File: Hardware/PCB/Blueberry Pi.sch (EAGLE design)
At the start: 172 parts, among them IC3 AT45DB161D, J1 TRANSFLASH-LOCK, J2 AUDIO_JACK_SMD, J3 40PINFPCH15-1LW, Q1 24Mhz, Q2 32kHz, X1 USB-B-S, X3 52745-2290

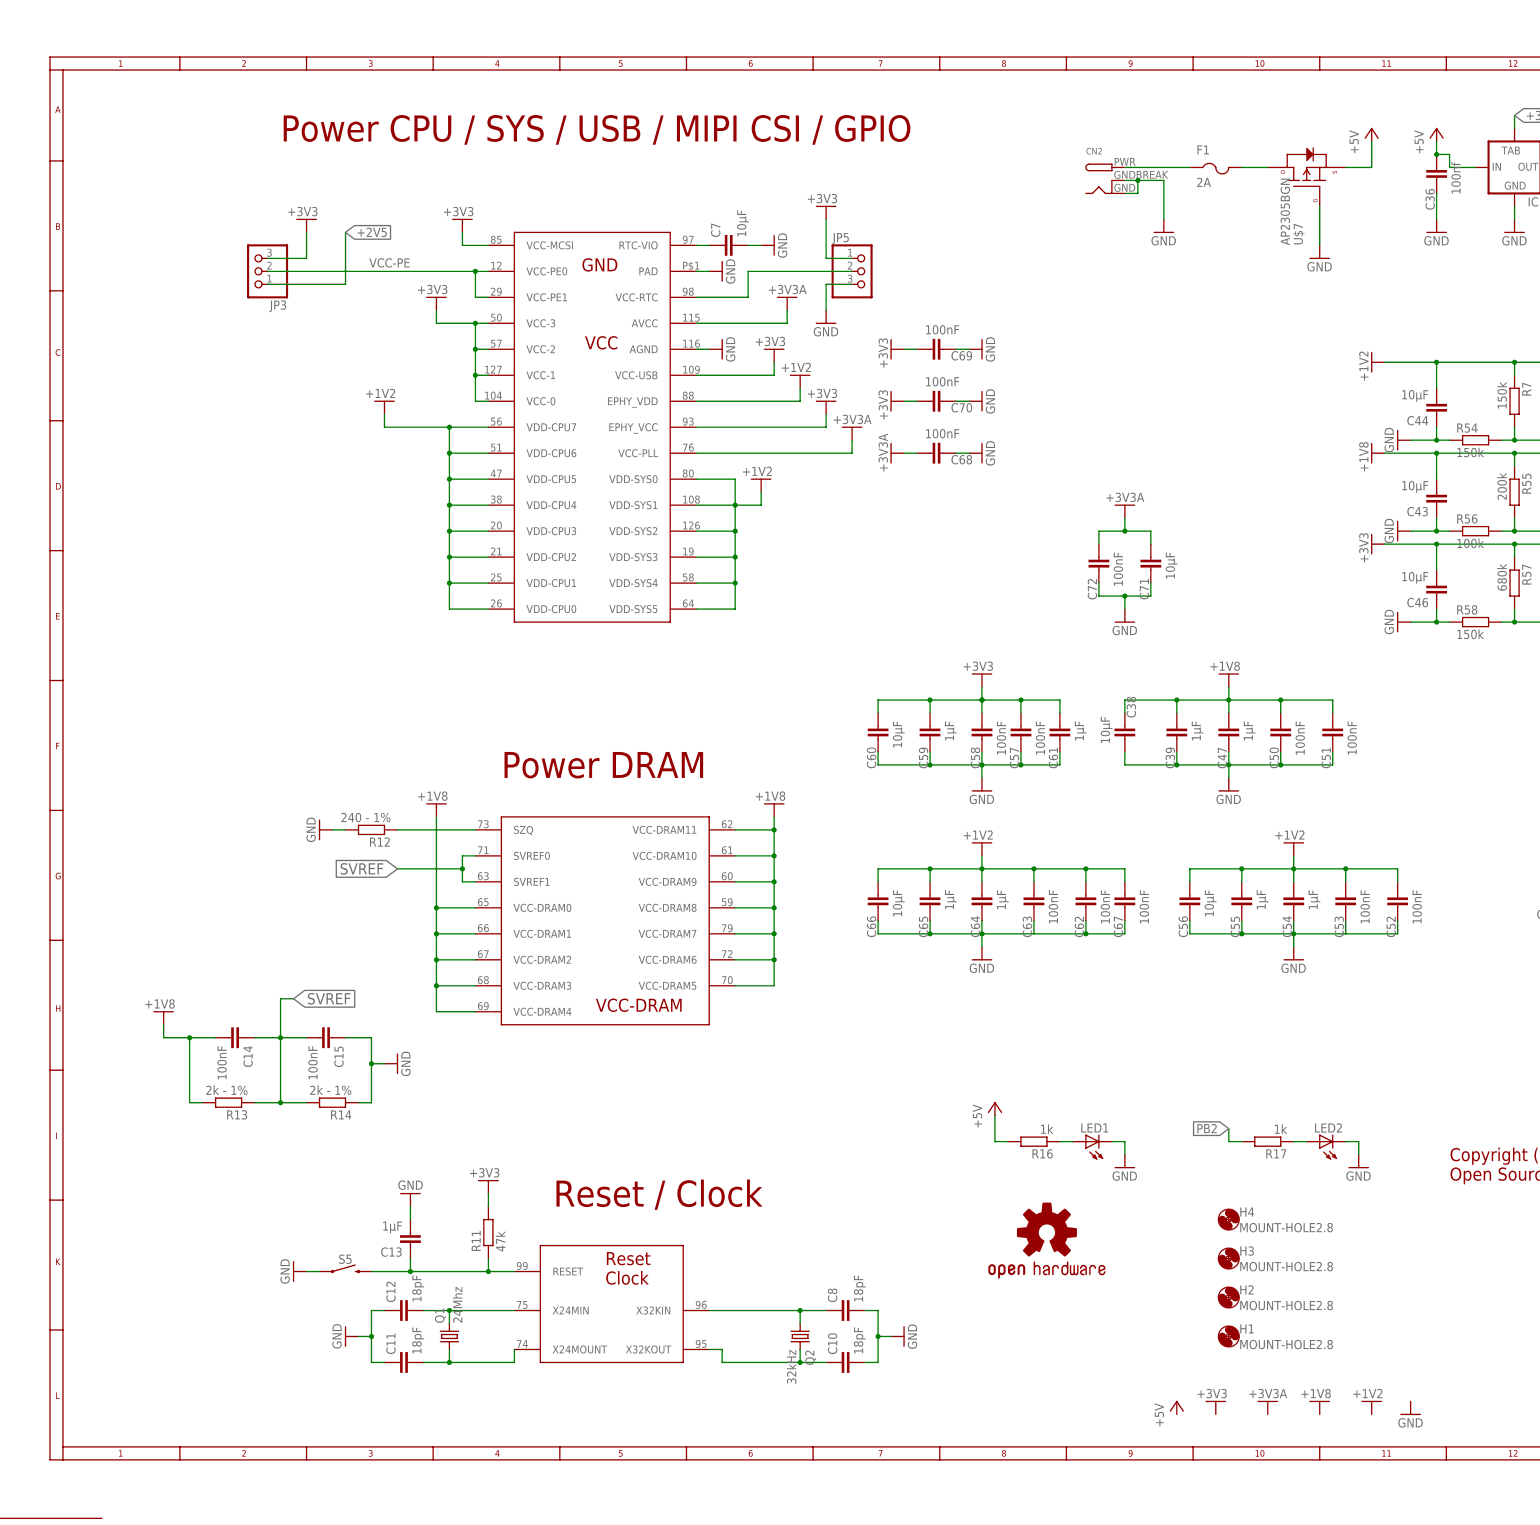
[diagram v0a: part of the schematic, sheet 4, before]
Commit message: updated schematics
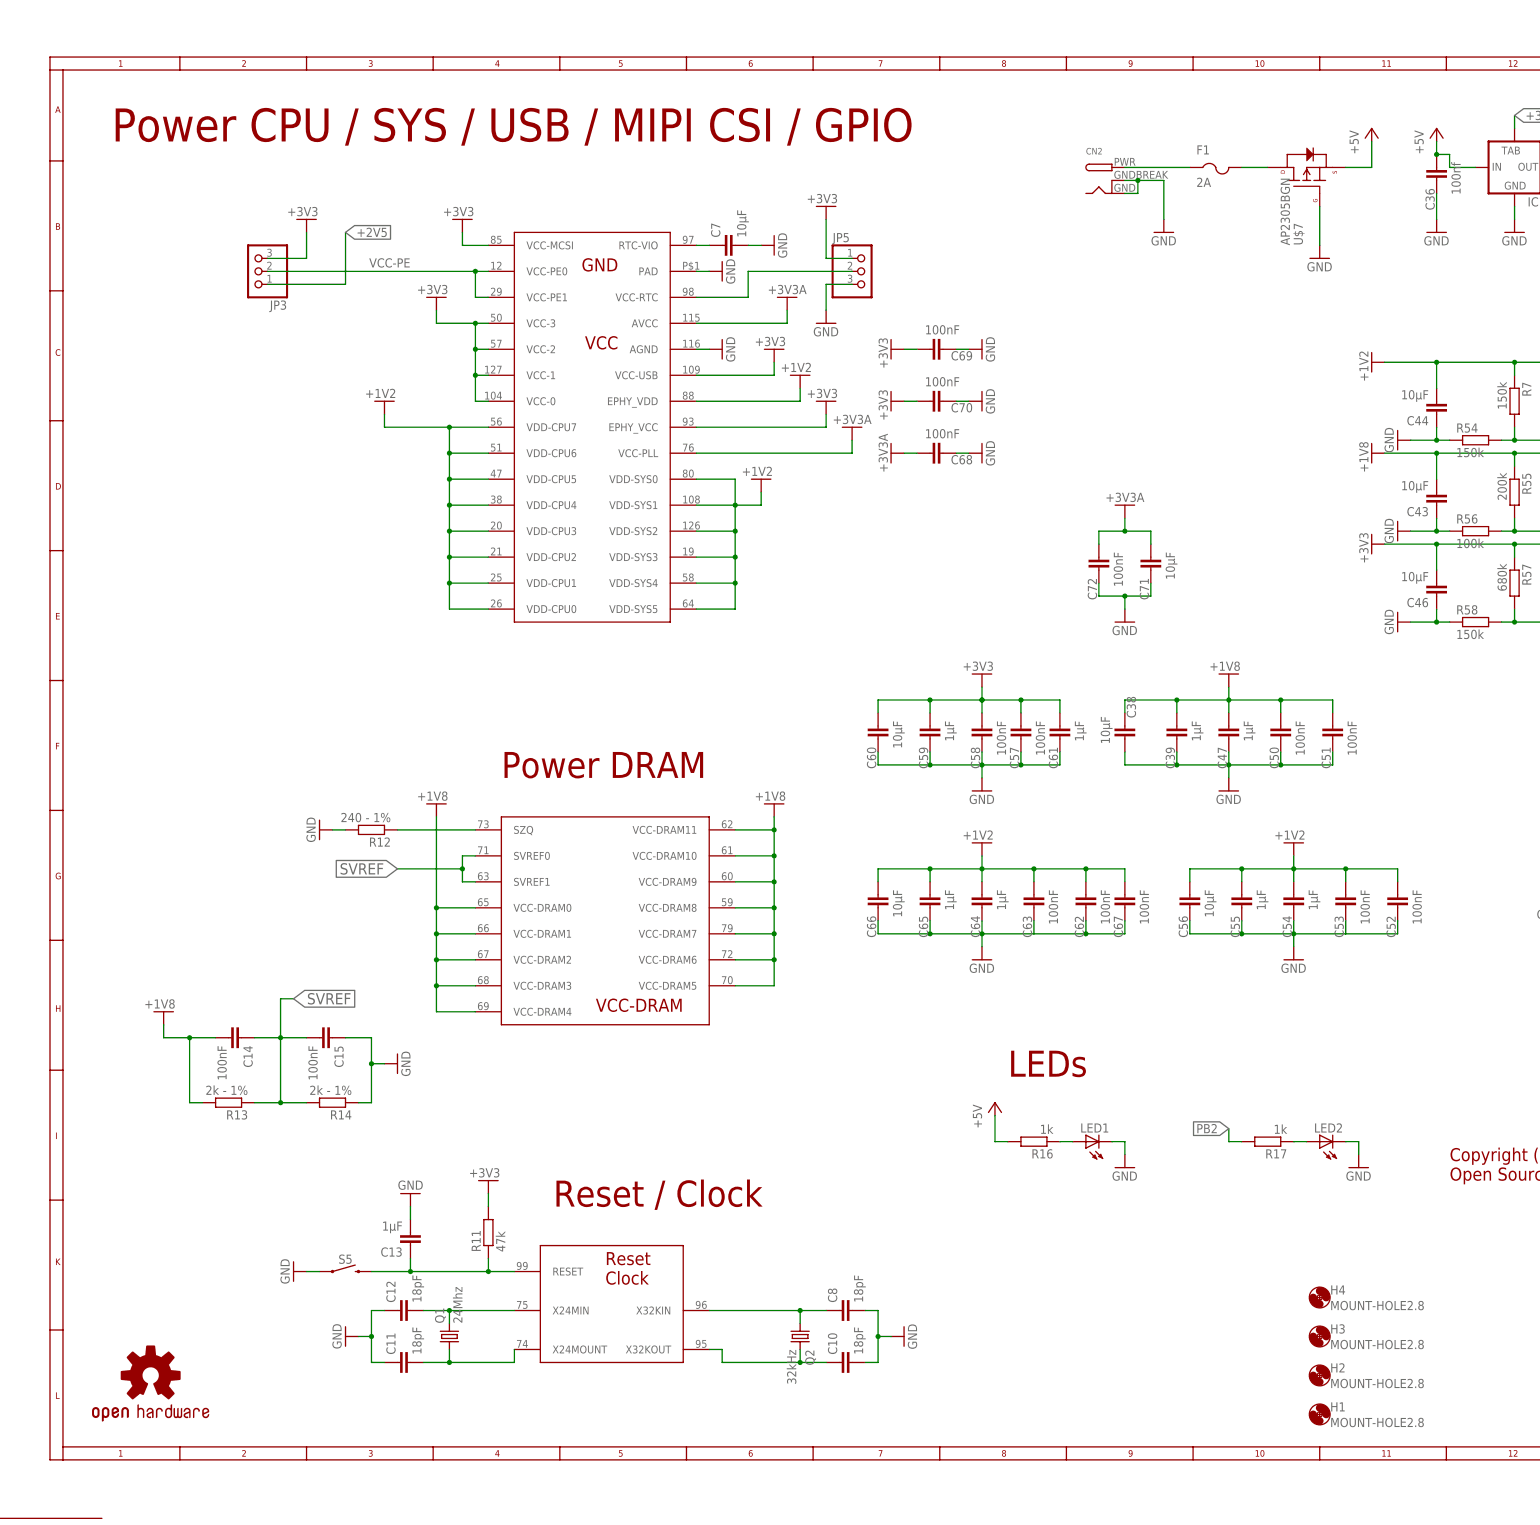
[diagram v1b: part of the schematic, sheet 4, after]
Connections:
- net UART2/RX renamed UART2/TX/PB0
- net UART2/TX renamed UART2/RX/PB1
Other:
- note added: "IO / LRADC / RTL8723BS / Touch / SPI Flash"
- note added: "IO / LRADC / RTL8723BS / Touch /SPI Flash"
- note added: "LCD FFC / Camera FFC / Camera Header (OV7670, OV2640)"
- note added: "LEDs"
- note added: "USB Device"
- note removed: "IO / LRADC / Video FFC / Camera FFC"
- moved on the sheet: C1, C17, C18, C2, C23, C24, C25, C26, C27, C28, C34, C48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
